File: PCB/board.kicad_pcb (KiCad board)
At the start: 2 copper layers, 169 parts, among them J1 Micro_SD_Card, J10 Conn_01x10, J11 Conn_01x02, J12 Conn_02x04_Odd_Even, J13 Conn_01x02, J14 Conn_01x02, J15 Conn_01x03, J16 Conn_01x02, J17 Conn_01x05, J18 Conn_01x04, J19 Conn_01x04, J2 Conn_ARM_JTAG_SWD_10, J20 Conn_01x02, J21 Conn_01x03, J22 Conn_02x04_Odd_Even, J23 Conn_01x04, J24 Conn_01x04, J25 Conn_01x02, J26 Conn_01x03, J27 Conn_02x04_Odd_Even, J28 Conn_01x04, J29 Conn_01x04, J3 USB_C_Receptacle_USB2.0_14P, J30 Conn_01x02, J31 Conn_01x03, J32 Conn_01x02, J33 Conn_01x02, J34 Conn_01x02, J35 Conn_01x02, J36 Conn_01x02, J37 Conn_01x02, J4 Conn_01x04, J5 Conn_01x04, J6 Conn_01x02, J7 Conn_01x03, J8 Conn_02x04_Odd_Even, J9 Conn_01x10, Q1 IRLML6402, Q2 NMOS, Q3 NMOS, Q4 NMOS, Q5 NMOS, Q6 NMOS, SW1 SW_Push, SW2 SW_Push, U1 STM32H743VITx, U2 LDO, U3 TPS54331, U4 TMC Stepstick, U5 TMC Stepstick, U6 TMC Stepstick, U7 TMC Stepstick, Y2 25 MHz

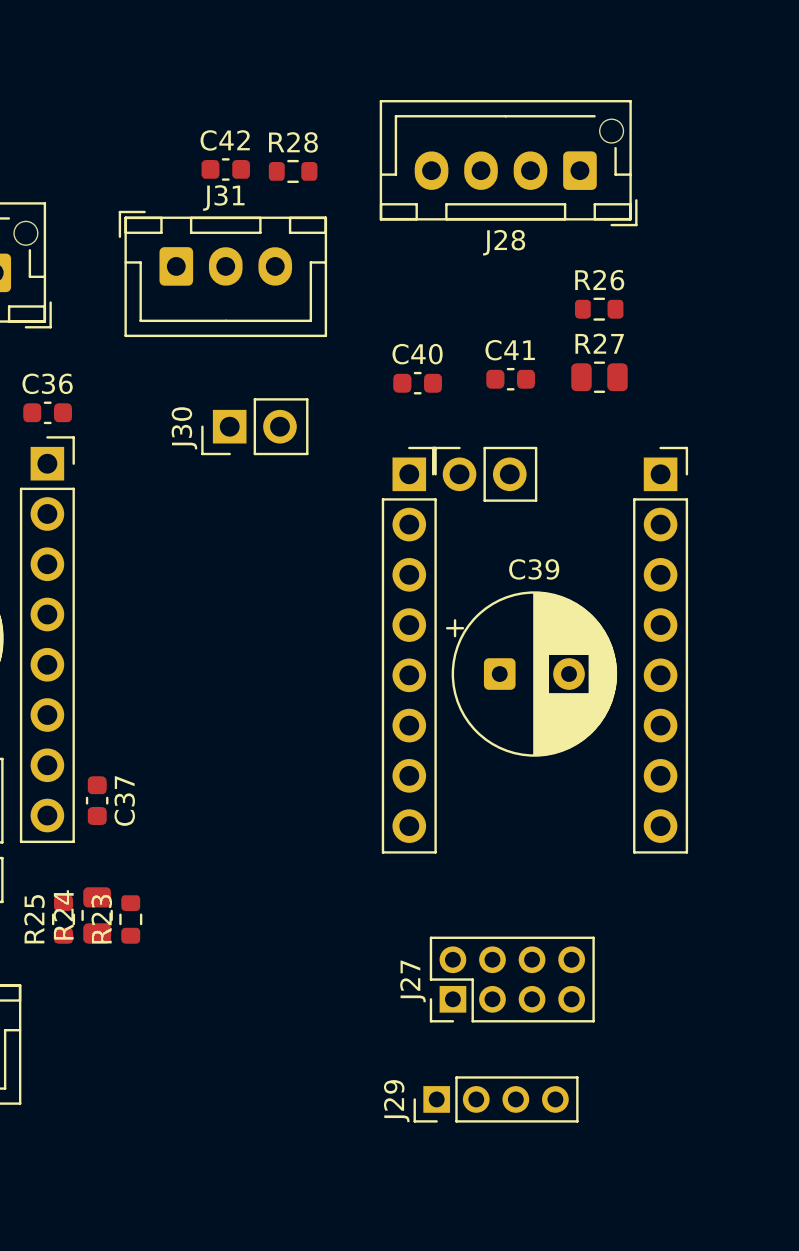
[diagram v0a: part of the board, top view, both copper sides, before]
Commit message: fourth driver
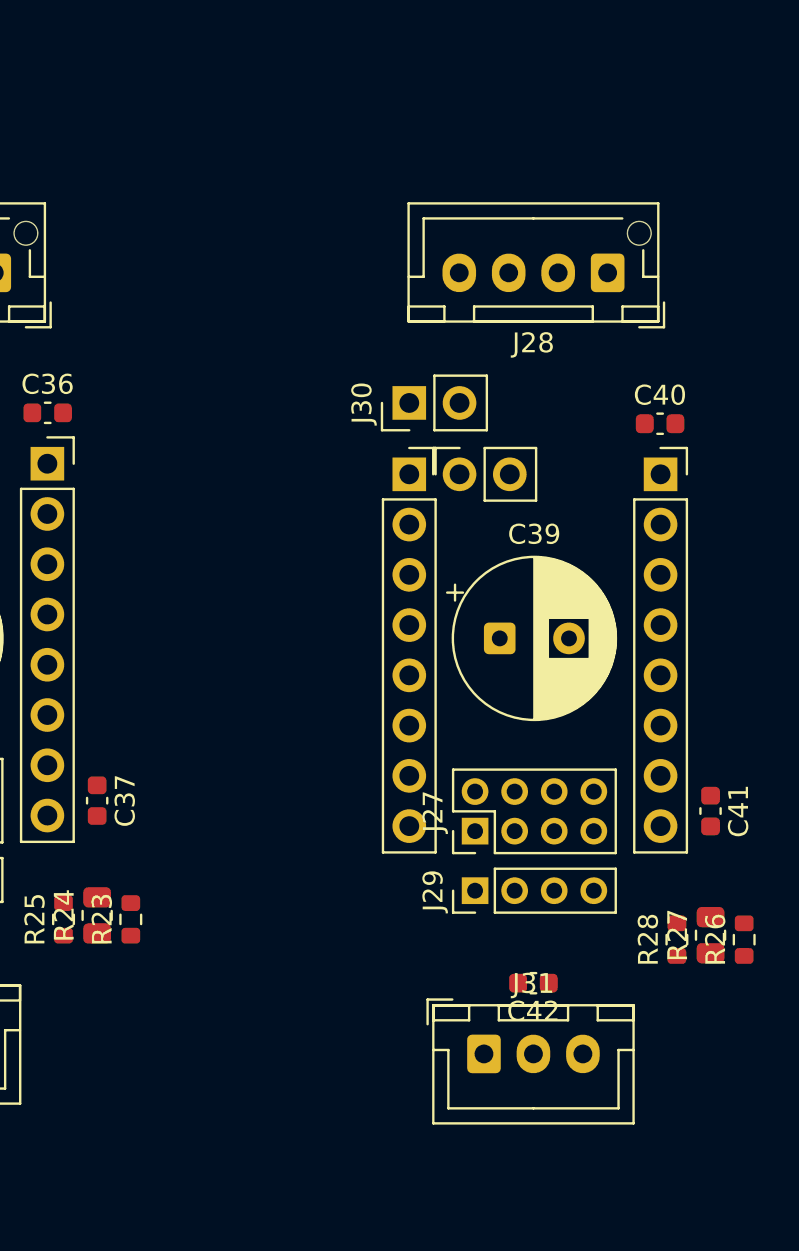
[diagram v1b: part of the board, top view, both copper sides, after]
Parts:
- moved C42 44.0 mm to (259.4, 66.4), turned to 180 degrees
- moved R28 43.4 mm to (266.7, 64.2), turned to 90 degrees
- moved J31 42.7 mm to (256.9, 70.0)
- moved R26 32.7 mm to (270.1, 64.2), turned to 90 degrees
- moved R27 28.8 mm to (268.4, 64.0), turned to 90 degrees
- moved C41 24.0 mm to (268.4, 57.7), turned to -90 degrees
- moved C40 12.4 mm to (265.9, 38.1)
- moved J29 10.7 mm to (256.5, 61.8)
- moved J30 9.15 mm to (253.2, 37.1)
- moved J27 8.57 mm to (256.5, 58.7)
- moved J28 5.35 mm to (263.2, 30.5)
- moved C39 1.80 mm to (257.7, 49.0)

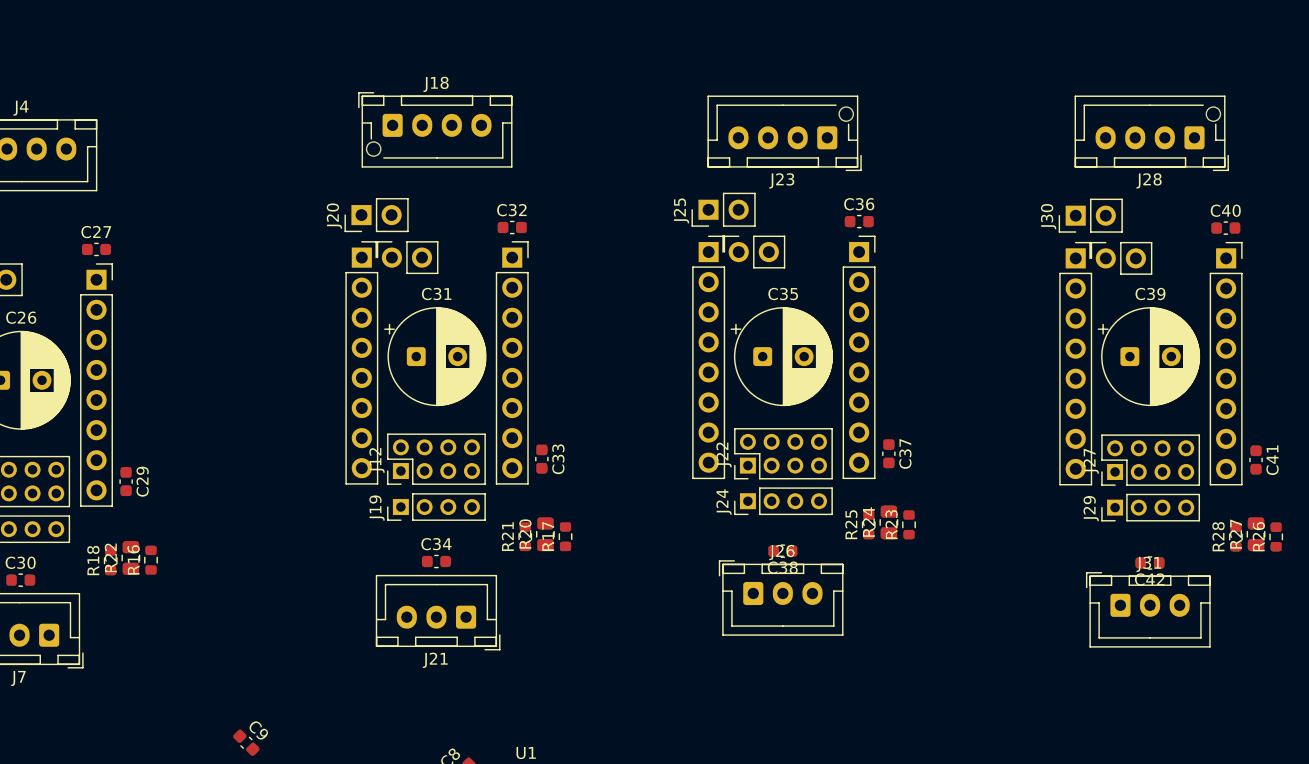
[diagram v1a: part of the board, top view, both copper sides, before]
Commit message: aligned all the motor drivers together
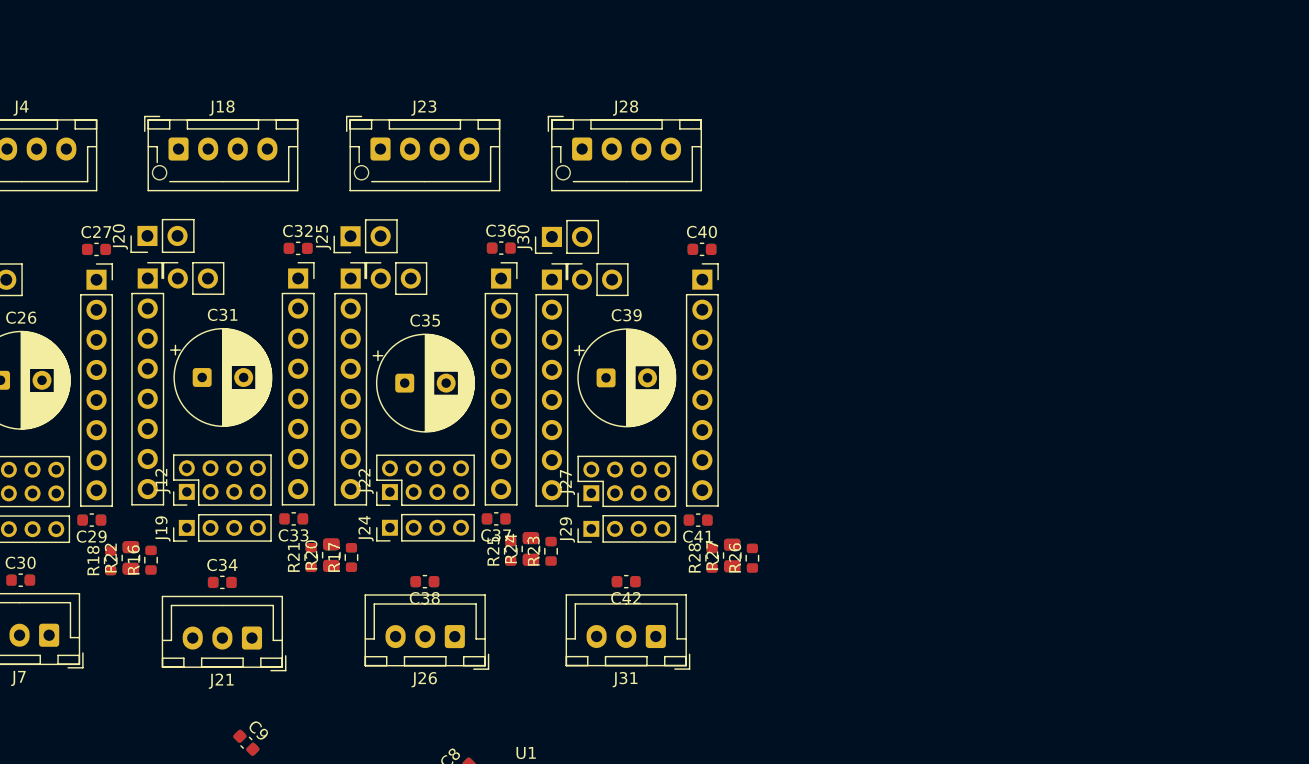
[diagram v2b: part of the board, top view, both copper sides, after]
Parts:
- moved J28 51.7 mm to (211.5, 31.5), turned to 0 degrees
- moved C41 47.4 mm to (221.3, 62.8), turned to 180 degrees
- moved C40 44.3 mm to (221.6, 39.9)
- moved J30 44.3 mm to (208.9, 38.9)
- moved R26 44.3 mm to (225.9, 66.0)
- moved U7 44.3 mm to (208.9, 42.5)
- moved C39 44.3 mm to (213.5, 50.8)
- moved J27 44.3 mm to (212.3, 60.5)
- moved J29 44.3 mm to (212.3, 63.5)
- moved R28 44.3 mm to (222.5, 66.0)
- moved R27 44.3 mm to (224.2, 65.8)
- moved C42 44.3 mm to (215.2, 68.0)
- moved J31 39.3 mm to (217.7, 72.6), turned to 180 degrees
- moved J23 37.7 mm to (194.5, 31.5), turned to 0 degrees
- moved C37 33.6 mm to (204.2, 62.7), turned to 180 degrees
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
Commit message: lots of organizing the power and displays
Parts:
- D1: footprint Diode_SMD:D_SMA -> Diode_SMD:D_SOD-123
- R10: footprint Resistor_SMD:R_0603_1608Metric -> Resistor_SMD:R_0805_2012Metric
- moved R47 210.9 mm to (50.2, 92.0), turned to 180 degrees
- moved J17 206.4 mm to (44.4, 101.8), turned to 90 degrees
- moved C28 204.8 mm to (49.5, 100.5), turned to -90 degrees
- moved C14 45.4 mm to (193.1, 76.0)
- moved J2 38.1 mm to (193.6, 78.4), turned to -90 degrees
- moved R8 28.7 mm to (33.7, 45.7)
- moved R48 24.1 mm to (33.7, 47.4)
- moved J3 23.6 mm to (26.4, 47.0)
- moved C44 22.4 mm to (39.0, 49.5)
- moved R10 19.5 mm to (53.3, 35.4), turned to -90 degrees
- moved R9 19.2 mm to (53.3, 27.6), turned to -90 degrees
- moved Q1 18.9 mm to (54.3, 31.5)
- moved D1 16.6 mm to (34.6, 49.5), turned to 180 degrees
- moved D2 10.9 mm to (41.4, 27.4)
- moved F1 7.48 mm to (36.2, 35.4), turned to 90 degrees
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
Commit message: hopping off cuz it's 3am...
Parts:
- C24: footprint Capacitor_SMD:CP_Elec_6.3x5.8 -> Capacitor_SMD:C_1210_3225Metric
- D1: footprint Diode_SMD:D_SOD-123 -> Diode_SMD:D_SMA
- moved C18 22.9 mm to (77.9, 32.8)
- moved C19 22.9 mm to (65.7, 35.0)
- moved U2 22.9 mm to (71.8, 32.6)
- moved C44 2.30 mm to (41.2, 50.0)
- moved D1 1.23 mm to (35.7, 50.0)

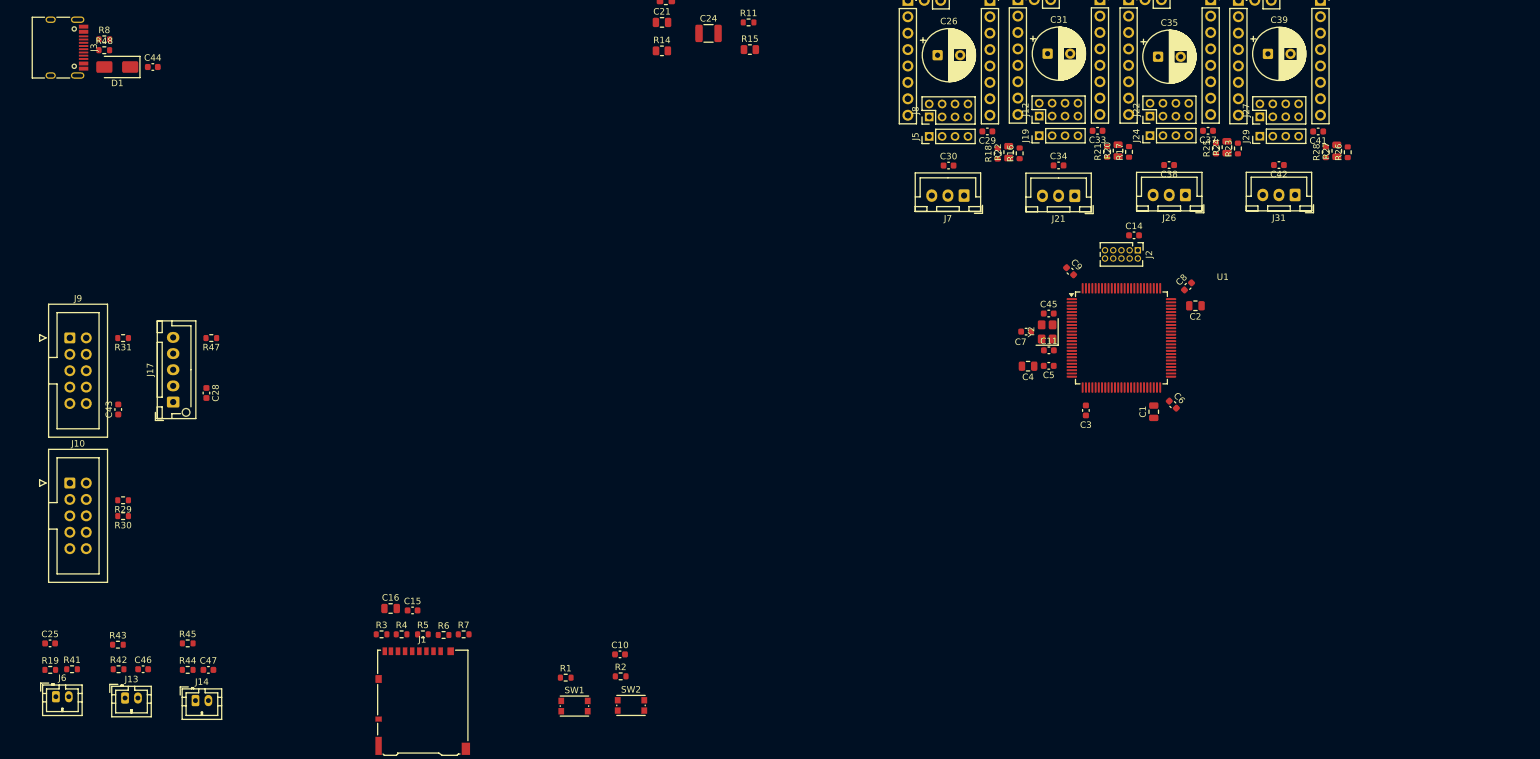
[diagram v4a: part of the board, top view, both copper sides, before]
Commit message: organized the thermistors
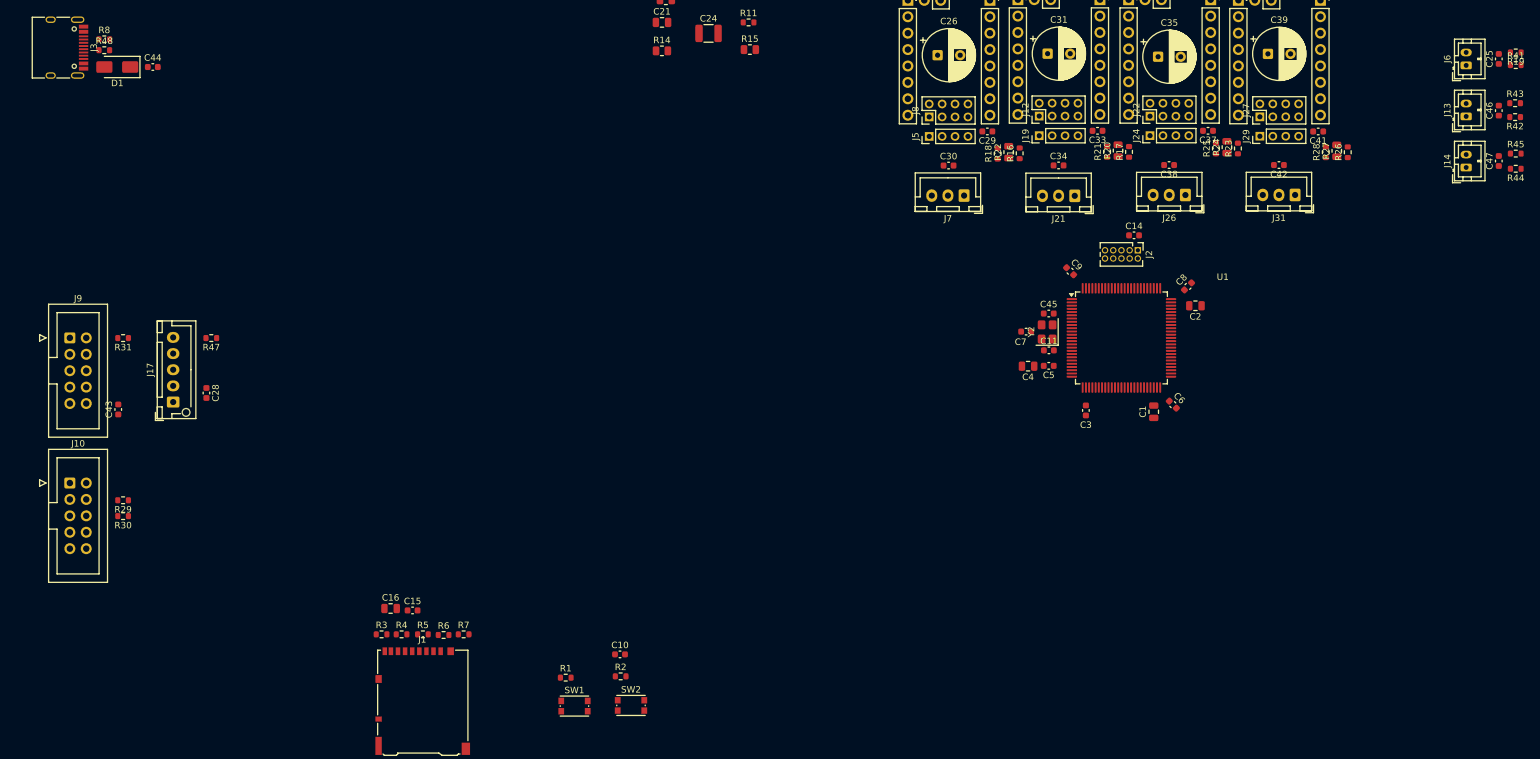
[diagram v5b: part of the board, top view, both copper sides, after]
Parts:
- moved R19 246.1 mm to (252.1, 47.8), turned to 180 degrees
- moved R41 242.2 mm to (252.1, 49.7)
- moved C25 241.8 mm to (249.5, 48.8), turned to 90 degrees
- moved J6 239.1 mm to (244.4, 49.8), turned to 90 degrees
- moved R42 232.4 mm to (252.0, 57.8), turned to 180 degrees
- moved R43 231.9 mm to (252.0, 55.6)
- moved C46 226.9 mm to (249.5, 56.8), turned to 90 degrees
- moved J13 226.2 mm to (244.4, 57.6), turned to 90 degrees
- moved R44 219.7 mm to (252.1, 65.8), turned to 180 degrees
- moved R45 219.1 mm to (252.1, 63.4)
- moved C47 214.7 mm to (249.5, 64.5), turned to 90 degrees
- moved J14 213.3 mm to (244.4, 65.5), turned to 90 degrees

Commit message: don't go to this commit, can't figure out 5V mosfet switching?
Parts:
- removed C13: 3.3nF, Capacitor_SMD:C_0805_2012Metric
- removed C20: 100pF, Capacitor_SMD:C_0603_1608Metric
- removed C21: 10nF, Capacitor_SMD:C_0805_2012Metric
- removed C22, C23: 0.1µF, Capacitor_SMD:C_0603_1608Metric
- removed C24: 47µF, Capacitor_SMD:C_1210_3225Metric
- removed D4: D_Schottky, Diode_SMD:D_SMA
- removed L2: 10µH, Inductor_SMD:L_Bourns-SRN8040_8x8.15mm
- removed R11: 10K, Resistor_SMD:R_0603_1608Metric
- removed R12: 100K, Resistor_SMD:R_0805_2012Metric
- removed R13: 11K, Resistor_SMD:R_0805_2012Metric
- removed R14: 56K, Resistor_SMD:R_0805_2012Metric
- removed R15: 53.6K, Resistor_SMD:R_0805_2012Metric
- removed U3: TPS54331, Package_SO:TI_SO-PowerPAD-8_ThermalVias
- added U8: AP63203WU, Package_TO_SOT_SMD:TSOT-23-6, F.Cu at (125.2, 38.8)
- C18, C19: value 10µF -> 4.7µF
- U2: value LDO -> AP7361C
- moved C18 1.05 mm to (79.0, 32.8)
- moved C19 1.00 mm to (64.7, 35.0)

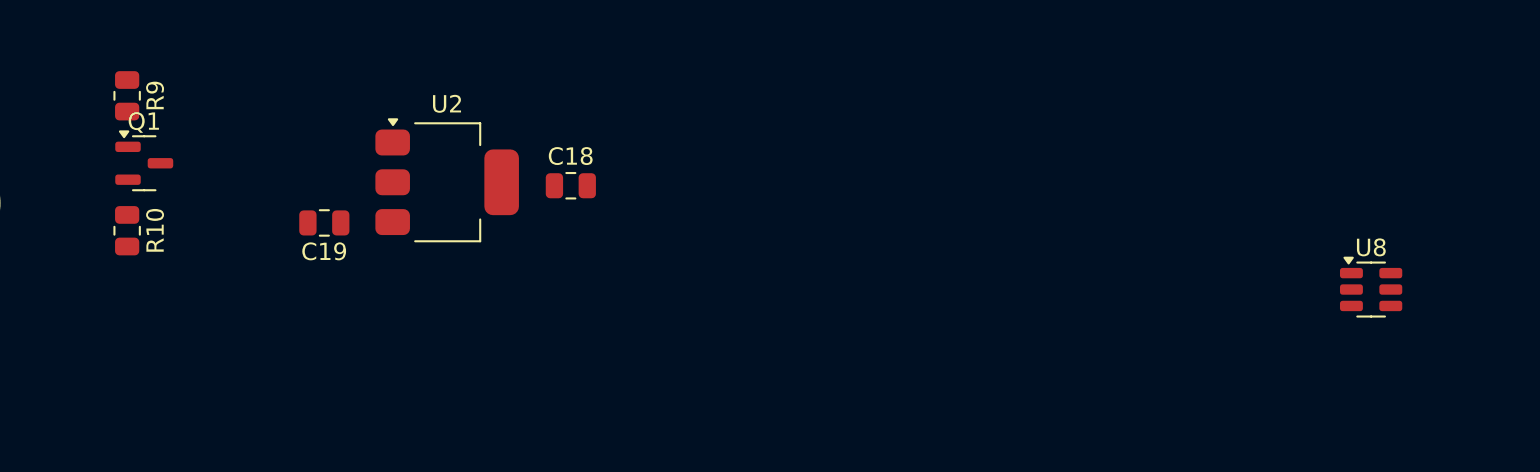
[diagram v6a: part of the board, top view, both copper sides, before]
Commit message: updated footprints for the buck converter
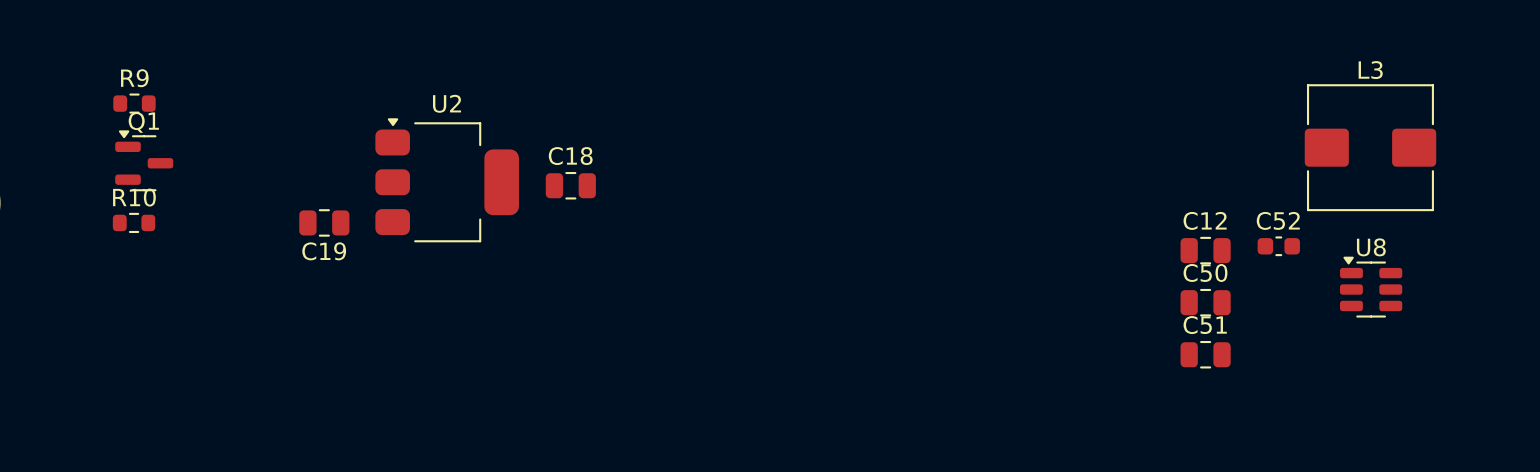
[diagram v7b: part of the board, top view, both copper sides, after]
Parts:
- added C12: 10µF, Capacitor_SMD:C_0805_2012Metric, F.Cu at (115.6, 36.5)
- added C50: 22µF, Capacitor_SMD:C_0805_2012Metric, F.Cu at (115.6, 39.6)
- added C51: 22µF, Capacitor_SMD:C_0805_2012Metric, F.Cu at (115.6, 42.6)
- added C52: 0.1µF, Capacitor_SMD:C_0603_1608Metric, F.Cu at (119.9, 36.3)
- added L3: 4.7µH, Inductor_SMD:L_Wuerth_HCM-7070, F.Cu at (125.2, 30.6)
- R10, R9: value 100K -> 10K; footprint Resistor_SMD:R_0805_2012Metric -> Resistor_SMD:R_0603_1608Metric
- moved R9 0.62 mm to (53.7, 28.1), turned to 0 degrees
- moved R10 0.60 mm to (53.7, 35.0), turned to 0 degrees
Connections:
- Q1 pad 2: 5V_USB -> 5V_PSU
- R9 pad 1: 5V_PSU -> 5V_USB
